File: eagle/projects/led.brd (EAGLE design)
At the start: 40 x 30 mm, 3 parts, among them X1 CLAMP_1X2-T-2.5MM

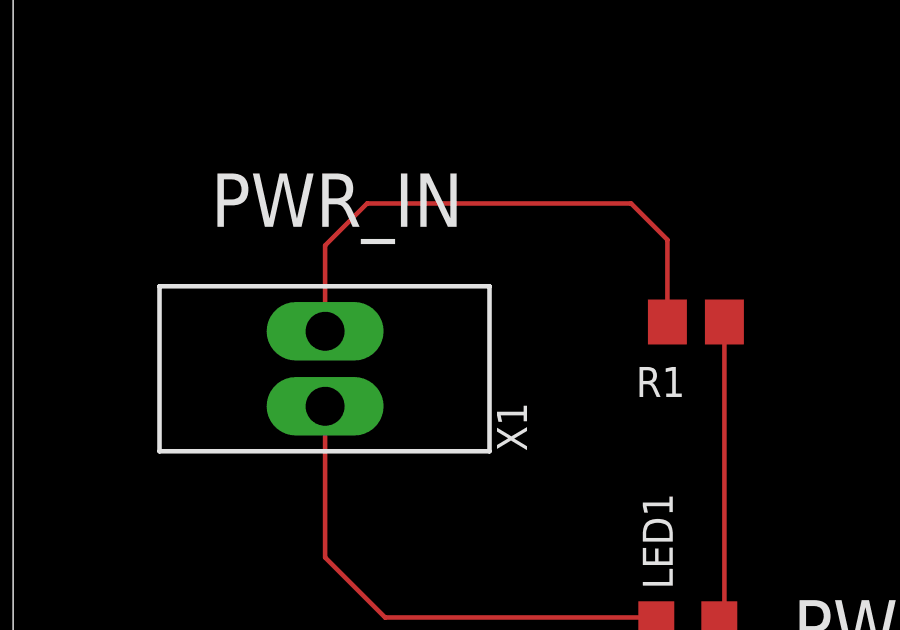
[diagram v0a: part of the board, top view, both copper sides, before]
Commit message: test buried vias
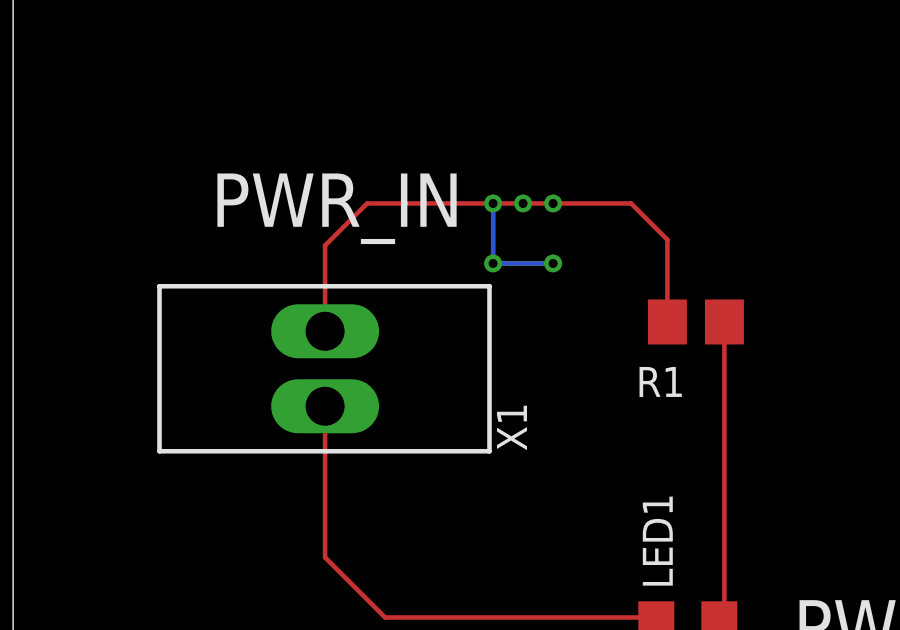
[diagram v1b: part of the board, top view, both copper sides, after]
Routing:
- net PWR_IN: track 18.1 -> 24.1 mm, vias 0 -> 6

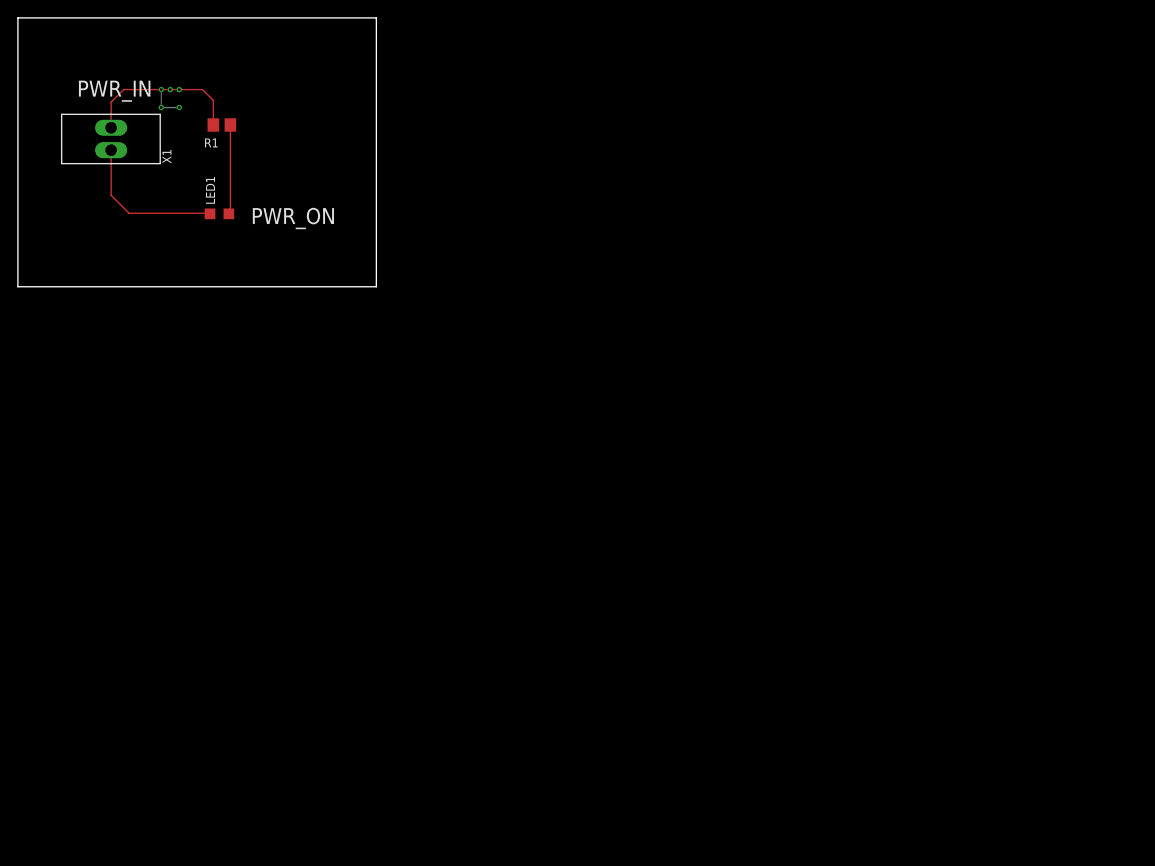
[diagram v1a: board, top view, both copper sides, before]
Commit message: added frame around layout
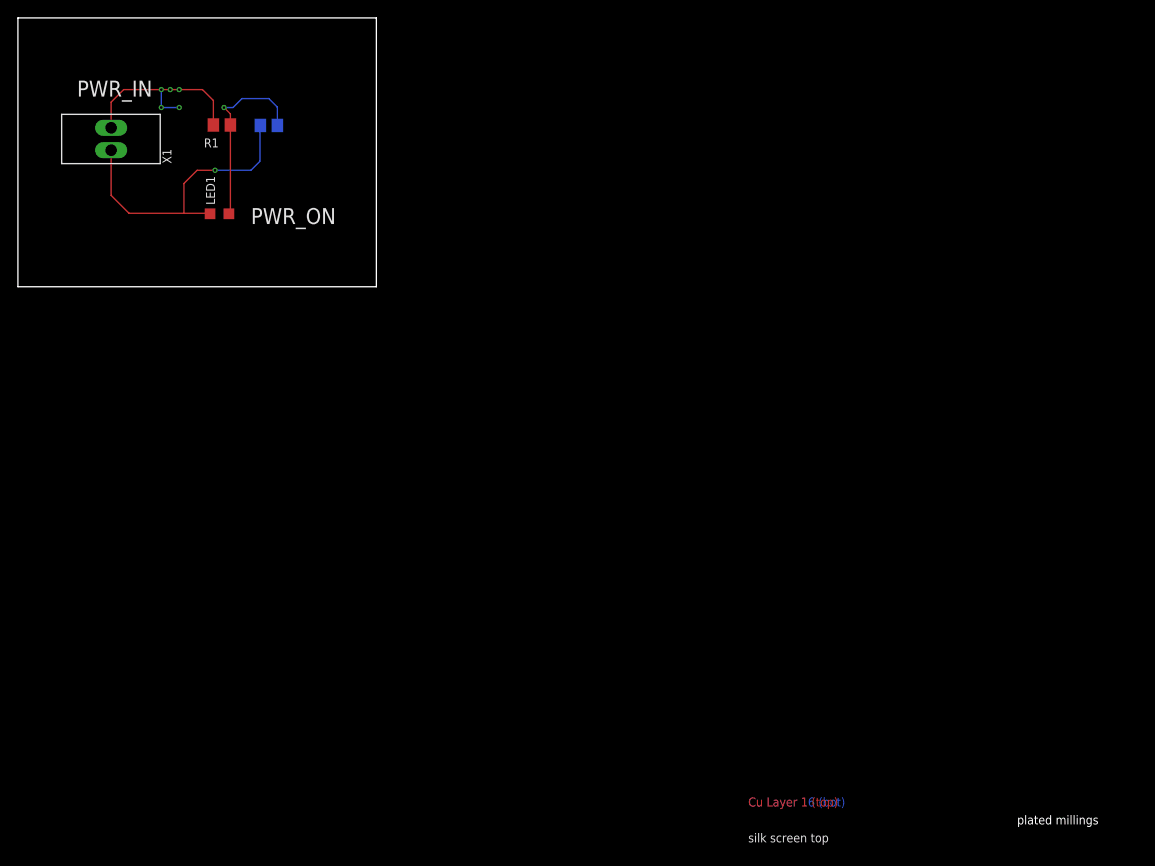
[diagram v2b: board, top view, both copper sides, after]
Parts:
- added R2: 330, be_rcl:S_0805
- added U$1: (no value), be_frame:A4_LANDSCAPE
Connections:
- net GND: now also R2.2
- net LED_A: now also R2.1
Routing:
- net GND: track 16.9 -> 33.8 mm, vias 0 -> 1
- net LED_A: track 9.98 -> 21.0 mm, vias 0 -> 1
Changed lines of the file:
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@@
 <layer number="45" name="Holes" color="7" fill="1" visible="no" active="yes"/>
 <layer number="46" name="Milling" color="3" fill="1" visible="no" active="yes"/>
-<layer number="47" name="Measures" color="7" fill="1" visible="no" active="yes"/>
+<layer number="47" name="Measures" color="7" fill="1" visible="yes" active="yes"/>
 <layer number="48" name="Document" color="7" fill="1" visible="yes" active="yes"/>
 <layer number="49" name="Reference" color="7" fill="1" visible="yes" active="yes"/>
@@
 <wire x1="40" y1="30" x2="0" y2="30" width="0" layer="20"/>
 <wire x1="0" y1="30" x2="0" y2="0" width="0" layer="20"/>
+<dimension x1="0" y1="30" x2="40" y2="30" x3="20" y3="34" textsize="1" textratio="13" layer="47"/>
+<dimension x1="40" y1="30" x2="40" y2="0" x3="46" y3="15" textsize="1" textratio="13" layer="47"/>
 </plain>
 <attributes>
@@
 <attribute name="UPDATED" value="" x="18" y="33" size="1.778" layer="27" rot="R90" display="off"/>
 </element>
+<element name="R2" library="be_rcl" package="S_0805" value="330" x="28" y="18" rot="MR0">
+<attribute name="PART_CODE_EXT" value="" x="28" y="18" size="1" layer="28" font="vector" ratio="13" rot="MR0" display="off"/>
+<attribute name="UPDATED" value="" x="28" y="18" size="1" layer="28" font="vector" ratio="13" rot="MR0" display="off"/>
+<attribute name="COMMISSIONED" value="2013-08-30" x="28" y="18" size="1" layer="28" font="vector" ratio="13" rot="MR0" display="off"/>
+<attribute name="PART_CODE_BEL" value="R_PAC_S_0805_VAL_330" x="28" y="18" size="1" layer="28" font="vector" ratio="13" rot="MR0" display="off"/>
+<attribute name="BOM" value="YES" x="28" y="18" size="1" layer="28" font="vector" ratio="13" rot="MR0" display="off"/>
+<attribute name="FUNCTION" value="" x="28" y="18" size="1" layer="28" font="vector" ratio="13" rot="MR0" display="off"/>
+</element>
+<element name="U$1" library="be_frame" package="A4_LANDSCAPE" value="" x="-71" y="-74"/>
 </elements>
 <signals>
@@
 <via x="18" y="20" extent="15-16" drill="0.3"/>
 <wire x1="16" y1="22" x2="16" y2="24" width="0.15" layer="15"/>
-<wire x1="16" y1="24" x2="18" y2="20" width="0" layer="19" extent="1-16"/>
 <via x="16" y="24" extent="2-15" drill="0.3"/>
 </signal>
@@
 <wire x1="23.71" y1="18.05" x2="23.71" y2="8.31" width="0.1524" layer="1"/>
 <wire x1="23.71" y1="8.31" x2="23.54" y2="8.14" width="0.1524" layer="1"/>
+<contactref element="R2" pad="1"/>
+<wire x1="28.95" y1="18" x2="28.95" y2="20.05" width="0.15" layer="16"/>
+<wire x1="28.95" y1="20.05" x2="28" y2="21" width="0.15" layer="16"/>
+<wire x1="28" y1="21" x2="25" y2="21" width="0.15" layer="16"/>
+<wire x1="25" y1="21" x2="24" y2="20" width="0.15" layer="16"/>
+<wire x1="24" y1="20" x2="23" y2="20" width="0.15" layer="16"/>
+<wire x1="23.71" y1="18.05" x2="23.71" y2="19.29" width="0.15" layer="1"/>
+<wire x1="23.71" y1="19.29" x2="23" y2="20" width="0.15" layer="1"/>
+<via x="23" y="20" extent="1-16" drill="0.3"/>
 </signal>
 <signal name="GND">
@@
 <wire x1="10.4" y1="15.24" x2="10.4" y2="10.2" width="0.1524" layer="1"/>
 <wire x1="10.4" y1="10.2" x2="12.4" y2="8.2" width="0.1524" layer="1"/>
-<wire x1="12.4" y1="8.2" x2="21.38" y2="8.2" width="0.1524" layer="1"/>
+<wire x1="12.4" y1="8.2" x2="18.523384375" y2="8.2" width="0.1524" layer="1"/>
+<wire x1="18.523384375" y1="8.2" x2="21.38" y2="8.2" width="0.1524" layer="1"/>
 <wire x1="21.38" y1="8.2" x2="21.44" y2="8.14" width="0.1524" layer="1"/>
+<contactref element="R2" pad="2"/>
+<wire x1="27.05" y1="18" x2="27" y2="18" width="0.15" layer="16"/>
+<wire x1="27" y1="18" x2="27" y2="14" width="0.15" layer="16"/>
+<wire x1="27" y1="14" x2="26" y2="13" width="0.15" layer="16"/>
+<wire x1="26" y1="13" x2="22" y2="13" width="0.15" layer="16"/>
+<wire x1="18.523384375" y1="8.2" x2="18.523384375" y2="11.523384375" width="0.15" layer="1"/>
+<wire x1="18.523384375" y1="11.523384375" x2="20" y2="13" width="0.15" layer="1"/>
+<wire x1="20" y1="13" x2="22" y2="13" width="0.15" layer="1"/>
+<via x="22" y="13" extent="1-16" drill="0.3"/>
 </signal>
 </signals>
 </board>
 </drawing>
+<compatibility>
+<note version="6.3" minversion="6.2.2" severity="warning">
+Since Version 6.2.2 text objects can contain more than one line,
+which will not be processed correctly with this version.
+</note>
+</compatibility>
 </eagle>
